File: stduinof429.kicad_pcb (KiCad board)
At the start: 2 copper layers, 94 x 56 mm, 67 parts, among them J1 Conn_02x03_Odd_Even, P1 Power, P10 CONN_02X20, P11 CONN_01X03, P12 USB_OTG, P2 Analog, P3 Digital, P4 Digital, P5 CONN_1, P6 CONN_1, P7 CONN_1, P8 CONN_1, P9 CONN_1, SW1 SW_PUSH, U1 AZ1117-3.3, U2 STM32F429IGTx

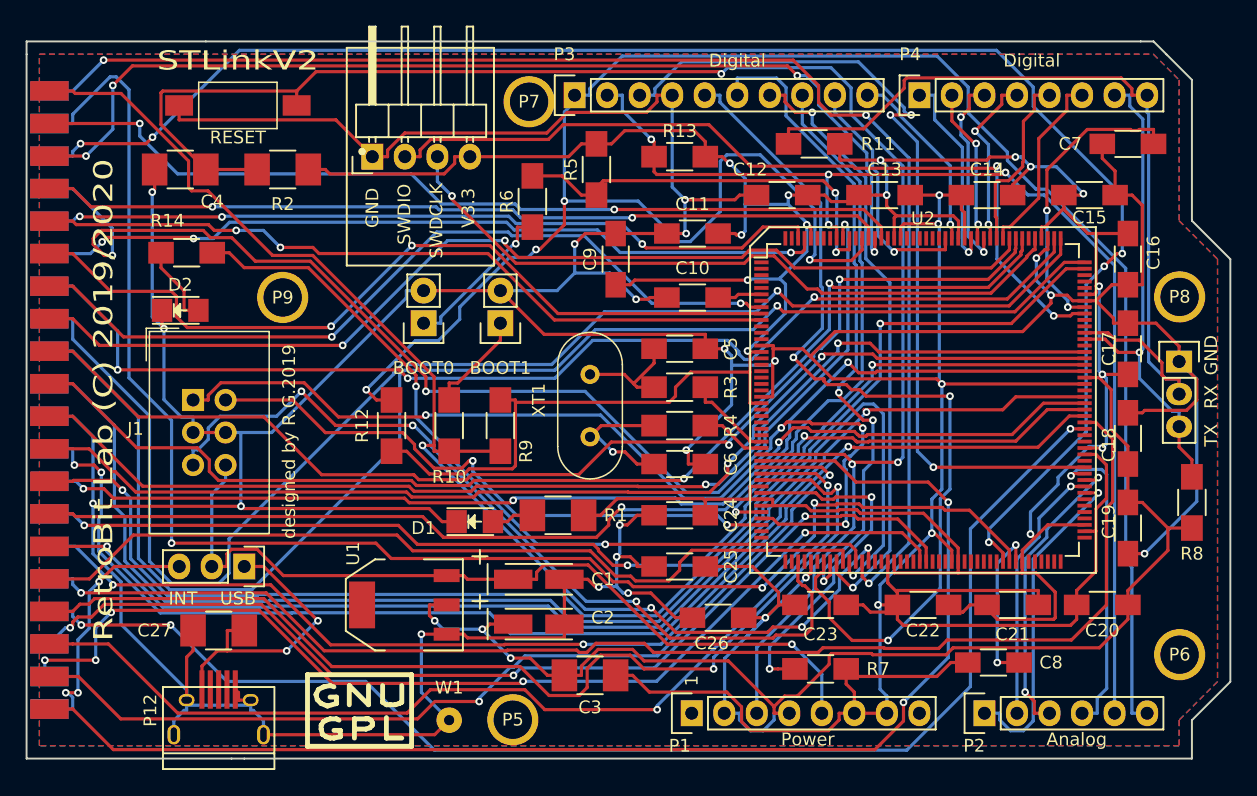
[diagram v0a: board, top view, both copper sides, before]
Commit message: Corrected pinout of lateral IDC 40 pin. Moved other bits to another port
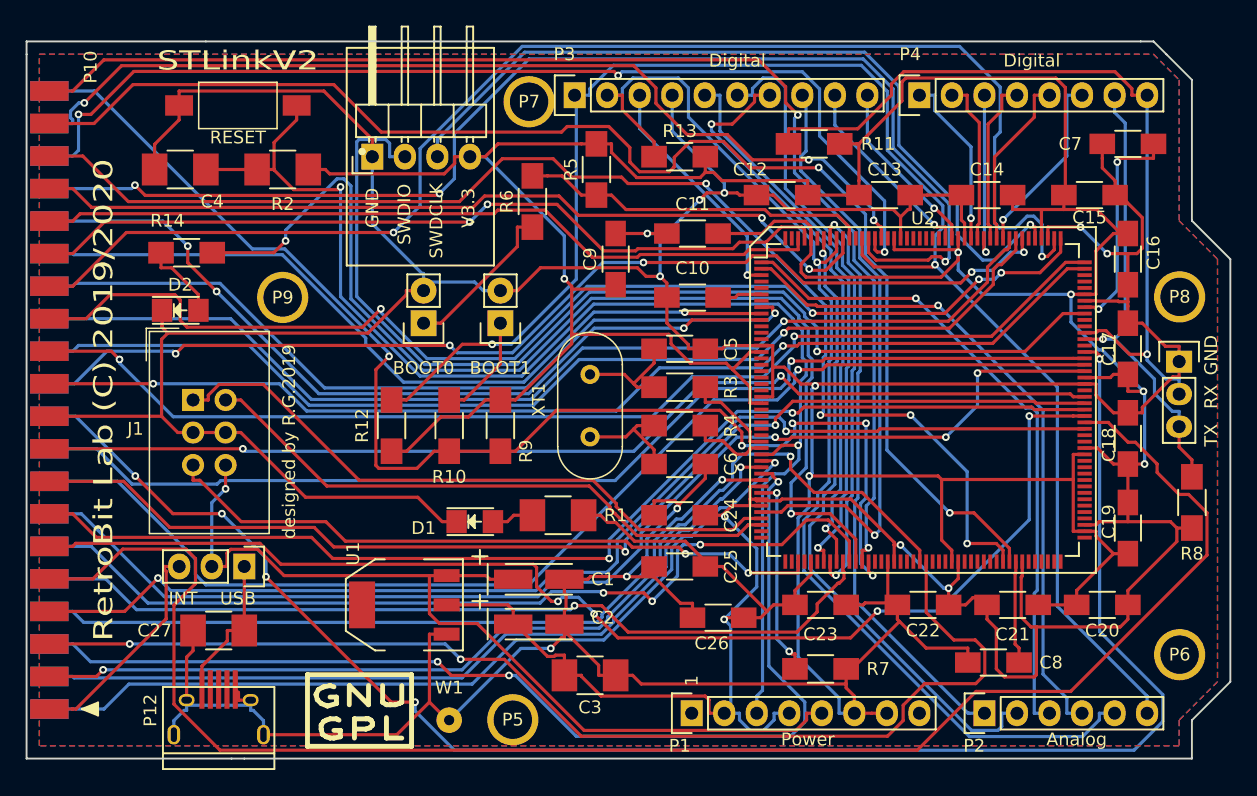
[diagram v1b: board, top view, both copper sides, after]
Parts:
- P10: moved to F.Cu
- turned P10 to 270 degrees
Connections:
- U2 pad 1: (no net) -> D10
- U2 pad 100: D12 -> (no net)
- U2 pad 169: (no net) -> D8
- U2 pad 170: (no net) -> D9
- U2 pad 2: (no net) -> D11
- U2 pad 3: (no net) -> D12
- U2 pad 96: D8 -> (no net)
- U2 pad 97: D9 -> (no net)
- U2 pad 98: D10 -> (no net)
- U2 pad 99: D11 -> (no net)
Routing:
- net GND: track 582.3 -> 475.3 mm, vias 24 -> 11
- net D12: track 66.8 -> 18.6 mm, vias 3 -> 1
- net mA9: track 89.4 -> 131.9 mm, vias 2 -> 5
- net I2C_SCL: track 160.7 -> 124.1 mm, vias 4 -> 2
- net mA0: track 103.4 -> 66.9 mm, vias 2 -> 1
- net ~mEXSEL: track 66.2 -> 96.8 mm, vias 2 -> 3
- net nRST: track 132.9 -> 102.8 mm, vias 3 -> 2
- net D9: track 20.5 -> 49.7 mm
- net SPI1_SCK: track 71.1 -> 43.1 mm, vias 3 -> 1
- net ~mMPD: track 95.2 -> 67.2 mm, vias 3 -> 2
- net D11: track 24.4 -> 52.3 mm
- net D10: track 23.4 -> 51.2 mm, vias 2 -> 1
- net ~mIRQ: track 126.8 -> 99.9 mm, vias 5 -> 4
- net mD3: track 103.3 -> 129.4 mm, vias 1 -> 0
- net SPI_SEL1: track 75.2 -> 50.3 mm, vias 4 -> 0
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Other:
- board text added: "https://github.com/gianlucarenzi/stduinof429"
- board text removed: "https://github.com/gianlucarenzi/quasiSTduino429"

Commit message: Rerouting with length match
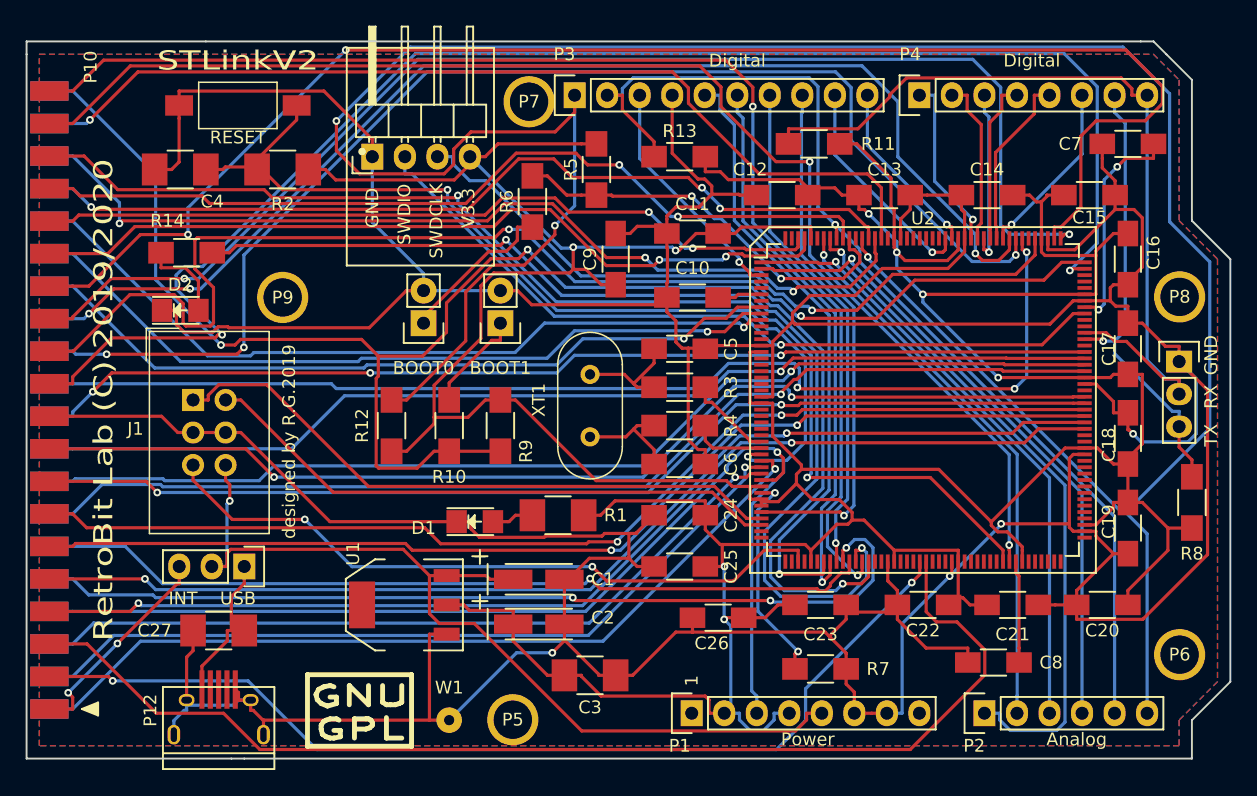
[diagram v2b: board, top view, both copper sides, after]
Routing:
- net I2C_SCL: track 124.1 -> 209.7 mm, vias 2 -> 3
- net mA9: track 131.9 -> 83.1 mm, vias 5 -> 3
- net mD3: track 129.4 -> 86.8 mm, vias 0 -> 2
- net mPHI2: track 86.3 -> 118.2 mm
- net mRD5: track 101.4 -> 130.3 mm, vias 5 -> 3
- net ~mEXSEL: track 96.8 -> 69.5 mm
- net mA2: track 84.5 -> 61.1 mm, vias 3 -> 1
- net SWDIO: track 82.8 -> 61.0 mm
- net GND: track 475.3 -> 491.5 mm, vias 11 -> 4
- net mA11: track 84.2 -> 99.0 mm, vias 1 -> 3
- net mD4: track 97.1 -> 85.7 mm, vias 4 -> 2
- net ~mS4: track 90.4 -> 100.9 mm, vias 4 -> 2
- net mA12: track 83.9 -> 94.1 mm, vias 1 -> 3
- net ~mS5: track 88.6 -> 98.3 mm
- net ~mD1XX: track 105.8 -> 114.9 mm
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
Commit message: Porting from Kicad 4 to Kicad 5
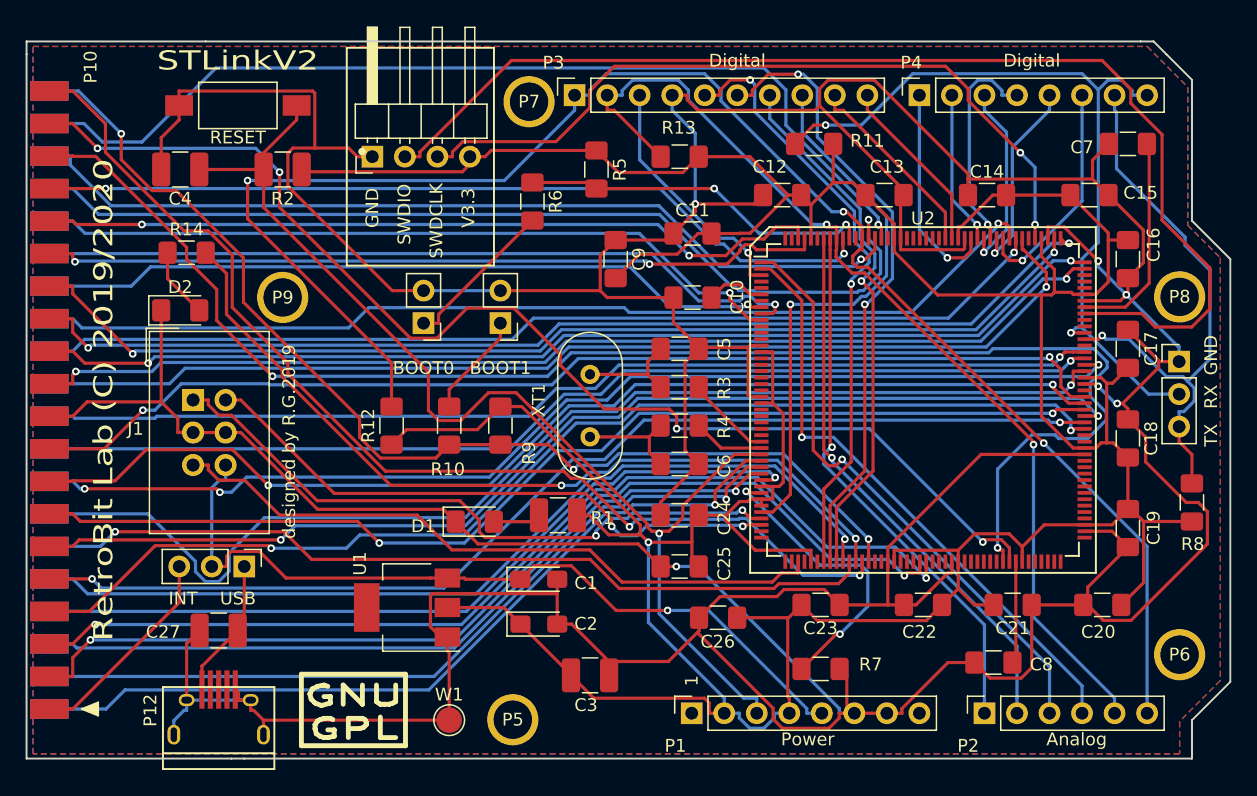
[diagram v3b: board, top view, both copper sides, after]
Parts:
- removed GPL: Symbol_GNU-GPL_CopperTop_Small, RetroBitLab:Symbol_GNU-GPL_SilkScreen_Small
- removed OSHW: OSHW-Logo2_14.6x12mm_SilkScreen, Symbol:OSHW-Logo2_14.6x12mm_SilkScreen
- added LDO: Symbol_GNU-GPL_CopperTop_Small, RetroBitLab:Symbol_GNU-GPL_SilkScreen_Small, F.Cu at (112.5, 123.8)
- added REF**: OSHW-Logo_11.4x12mm_SilkScreen, Symbol:OSHW-Logo_11.4x12mm_SilkScreen, B.Cu at (156.2, 97.4)
- BOOT0_MEM1, BOOT1_MEM1: footprint Pin_Headers:Pin_Header_Straight_1x02 -> Connector_PinHeader_2.54mm:PinHeader_1x02_P2.54mm_Vertical
- C1, C2: footprint Capacitors_Tantalum_SMD:TantalC_SizeA_EIA-3216_HandSoldering -> Capacitor_Tantalum_SMD:CP_EIA-3216-18_Kemet-A_Pad1.58x1.35mm_HandSolder
- C10, C11, C12, C13, C14, C15, C16, C17, C18, C19, C20, C21, C22, C23, C24, C25, C26, C5, C6, C7, C8, C9: footprint Capacitors_SMD:C_1206_HandSoldering -> Capacitor_SMD:C_1206_3216Metric_Pad1.42x1.75mm_HandSolder
- C27, C3, C4: footprint Capacitors_SMD:C_1210_HandSoldering -> Capacitor_SMD:C_1210_3225Metric_Pad1.42x2.65mm_HandSolder
- D1, D2: footprint LEDs:LED_1206 -> LED_SMD:LED_1206_3216Metric_Pad1.42x1.75mm_HandSolder
- DEBUG1, P11: footprint Pin_Headers:Pin_Header_Straight_1x03 -> Connector_PinHeader_2.54mm:PinHeader_1x03_P2.54mm_Vertical
- P1, P4: footprint Socket_Strips:Socket_Strip_Straight_1x08 -> Connector_PinSocket_2.54mm:PinSocket_1x08_P2.54mm_Vertical
- P2: footprint Socket_Strips:Socket_Strip_Straight_1x06 -> Connector_PinSocket_2.54mm:PinSocket_1x06_P2.54mm_Vertical
- P3: footprint Socket_Strips:Socket_Strip_Straight_1x10 -> Connector_PinSocket_2.54mm:PinSocket_1x10_P2.54mm_Vertical
- R1, R2: footprint Resistors_SMD:R_1210_HandSoldering -> Resistor_SMD:R_1210_3225Metric_Pad1.42x2.65mm_HandSolder
- R10, R11, R12, R13, R14, R3, R4, R5, R6, R7, R8, R9: footprint Resistors_SMD:R_1206_HandSoldering -> Resistor_SMD:R_1206_3216Metric_Pad1.42x1.75mm_HandSolder
- SWDIO/CLK1: footprint Pin_Headers:Pin_Header_Angled_1x04 -> Connector_PinHeader_2.54mm:PinHeader_1x04_P2.54mm_Horizontal
- U1: footprint TO_SOT_Packages_SMD:SOT-223 -> Package_TO_SOT_SMD:SOT-223
- U2: footprint Housings_QFP:LQFP-176_24x24mm_Pitch0.5mm -> Package_QFP:LQFP-176_24x24mm_P0.5mm
- W1: footprint Wire_Pads:SolderWirePad_single_0-8mmDrill -> TestPoint:TestPoint_Pad_D2.0mm
- moved U1 0.30 mm to (116.7, 115.6), turned to 180 degrees
- turned P1 to 90 degrees
- turned P2 to 90 degrees
- turned P3 to 90 degrees
- turned P4 to 90 degrees
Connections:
- P1 pad 1: (no net) -> Net-(P1-Pad1)
- P1 pad 8: (no net) -> /Vin
- P12 pad 2: (no net) -> Net-(P12-Pad2)
- P12 pad 3: (no net) -> Net-(P12-Pad3)
- P12 pad 4: (no net) -> Net-(P12-Pad4)
- P5 pad 1: (no net) -> Net-(P5-Pad1)
- P6 pad 1: (no net) -> Net-(P6-Pad1)
- P7 pad 1: (no net) -> Net-(P7-Pad1)
- P8 pad 1: (no net) -> Net-(P8-Pad1)
- P9 pad 1: (no net) -> Net-(P9-Pad1)
- U2 pad 100: (no net) -> Net-(U2-Pad100)
- U2 pad 101: (no net) -> Net-(U2-Pad101)
- U2 pad 104: (no net) -> Net-(U2-Pad104)
- U2 pad 105: (no net) -> Net-(U2-Pad105)
- U2 pad 11: (no net) -> Net-(U2-Pad11)
- U2 pad 112: (no net) -> Net-(U2-Pad112)
- U2 pad 119: (no net) -> Net-(U2-Pad119)
- U2 pad 12: (no net) -> Net-(U2-Pad12)
- U2 pad 122: (no net) -> Net-(U2-Pad122)
- U2 pad 123: (no net) -> Net-(U2-Pad123)
- U2 pad 128: (no net) -> Net-(U2-Pad128)
- U2 pad 129: (no net) -> Net-(U2-Pad129)
- U2 pad 13: (no net) -> Net-(U2-Pad13)
- U2 pad 130: (no net) -> Net-(U2-Pad130)
- U2 pad 138: (no net) -> Net-(U2-Pad138)
- U2 pad 152: (no net) -> Net-(U2-Pad152)
- U2 pad 153: (no net) -> Net-(U2-Pad153)
- U2 pad 154: (no net) -> Net-(U2-Pad154)
- U2 pad 155: (no net) -> Net-(U2-Pad155)
- U2 pad 156: (no net) -> Net-(U2-Pad156)
- U2 pad 157: (no net) -> Net-(U2-Pad157)
- U2 pad 16: (no net) -> Net-(U2-Pad16)
- U2 pad 160: (no net) -> Net-(U2-Pad160)
- U2 pad 165: (no net) -> Net-(U2-Pad165)
- U2 pad 17: (no net) -> Net-(U2-Pad17)
- U2 pad 171: (no net) -> Net-(U2-Pad171)
- U2 pad 175: (no net) -> Net-(U2-Pad175)
- U2 pad 176: (no net) -> Net-(U2-Pad176)
- U2 pad 18: (no net) -> Net-(U2-Pad18)
- U2 pad 19: (no net) -> Net-(U2-Pad19)
- U2 pad 20: (no net) -> Net-(U2-Pad20)
- U2 pad 21: (no net) -> Net-(U2-Pad21)
- U2 pad 24: (no net) -> Net-(U2-Pad24)
- U2 pad 25: (no net) -> Net-(U2-Pad25)
- U2 pad 26: (no net) -> Net-(U2-Pad26)
- U2 pad 27: (no net) -> Net-(U2-Pad27)
- U2 pad 28: (no net) -> Net-(U2-Pad28)
- U2 pad 4: (no net) -> Net-(U2-Pad4)
- U2 pad 43: (no net) -> Net-(U2-Pad43)
- U2 pad 44: (no net) -> Net-(U2-Pad44)
- U2 pad 45: (no net) -> Net-(U2-Pad45)
- U2 pad 46: (no net) -> Net-(U2-Pad46)
- U2 pad 48: (no net) -> Net-(U2-Pad48)
- U2 pad 5: (no net) -> Net-(U2-Pad5)
- U2 pad 50: (no net) -> Net-(U2-Pad50)
- U2 pad 59: (no net) -> Net-(U2-Pad59)
- U2 pad 60: (no net) -> Net-(U2-Pad60)
- U2 pad 63: (no net) -> Net-(U2-Pad63)
- U2 pad 64: (no net) -> Net-(U2-Pad64)
- U2 pad 65: (no net) -> Net-(U2-Pad65)
- U2 pad 68: (no net) -> Net-(U2-Pad68)
- U2 pad 69: (no net) -> Net-(U2-Pad69)
- U2 pad 7: (no net) -> Net-(U2-Pad7)
- U2 pad 70: (no net) -> Net-(U2-Pad70)
- U2 pad 73: (no net) -> Net-(U2-Pad73)
- U2 pad 74: (no net) -> Net-(U2-Pad74)
- U2 pad 75: (no net) -> Net-(U2-Pad75)
- U2 pad 76: (no net) -> Net-(U2-Pad76)
- U2 pad 77: (no net) -> Net-(U2-Pad77)
- U2 pad 78: (no net) -> Net-(U2-Pad78)
- U2 pad 83: (no net) -> Net-(U2-Pad83)
- U2 pad 84: (no net) -> Net-(U2-Pad84)
- U2 pad 85: (no net) -> Net-(U2-Pad85)
- U2 pad 86: (no net) -> Net-(U2-Pad86)
- U2 pad 87: (no net) -> Net-(U2-Pad87)
- U2 pad 88: (no net) -> Net-(U2-Pad88)
- U2 pad 89: (no net) -> Net-(U2-Pad89)
- U2 pad 92: (no net) -> Net-(U2-Pad92)
- U2 pad 93: (no net) -> Net-(U2-Pad93)
- U2 pad 94: (no net) -> Net-(U2-Pad94)
- U2 pad 95: (no net) -> Net-(U2-Pad95)
- U2 pad 96: (no net) -> Net-(U2-Pad96)
- U2 pad 97: (no net) -> Net-(U2-Pad97)
- U2 pad 98: (no net) -> Net-(U2-Pad98)
- U2 pad 99: (no net) -> Net-(U2-Pad99)
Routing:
- net I2C_SCL: track 209.7 -> 128.5 mm
- net VCC_3V3: track 397.2 -> 336.9 mm, vias 8 -> 1
- net mRD5: track 130.3 -> 86.2 mm
- net mPHI2: track 118.2 -> 85.1 mm
- net SWDIO: track 61.0 -> 91.5 mm, vias 1 -> 0
- net ~mD1XX: track 114.9 -> 85.4 mm
- net ~mIRQ: track 94.7 -> 116.6 mm
- net GND: track 491.5 -> 512.2 mm, vias 4 -> 6
- net mA11: track 99.0 -> 79.7 mm, vias 3 -> 1
- net LEDGRN_MEM: track 83.7 -> 65.6 mm
- net ~mRST: track 100.6 -> 84.8 mm
- net ~mS4: track 100.9 -> 85.4 mm
- net mA12: track 94.1 -> 80.1 mm, vias 3 -> 1
- net ~mS5: track 98.3 -> 84.6 mm
- net mD1: track 90.6 -> 78.4 mm, vias 0 -> 2
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
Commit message: Added without the packages/kicad folder needed. All stuff is now on kicad sources and RetroBitLab Library
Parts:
- removed LDO: Symbol_GNU-GPL_CopperTop_Small, RetroBitLab:Symbol_GNU-GPL_SilkScreen_Small
- removed REF**: OSHW-Logo_11.4x12mm_SilkScreen, Symbol:OSHW-Logo_11.4x12mm_SilkScreen

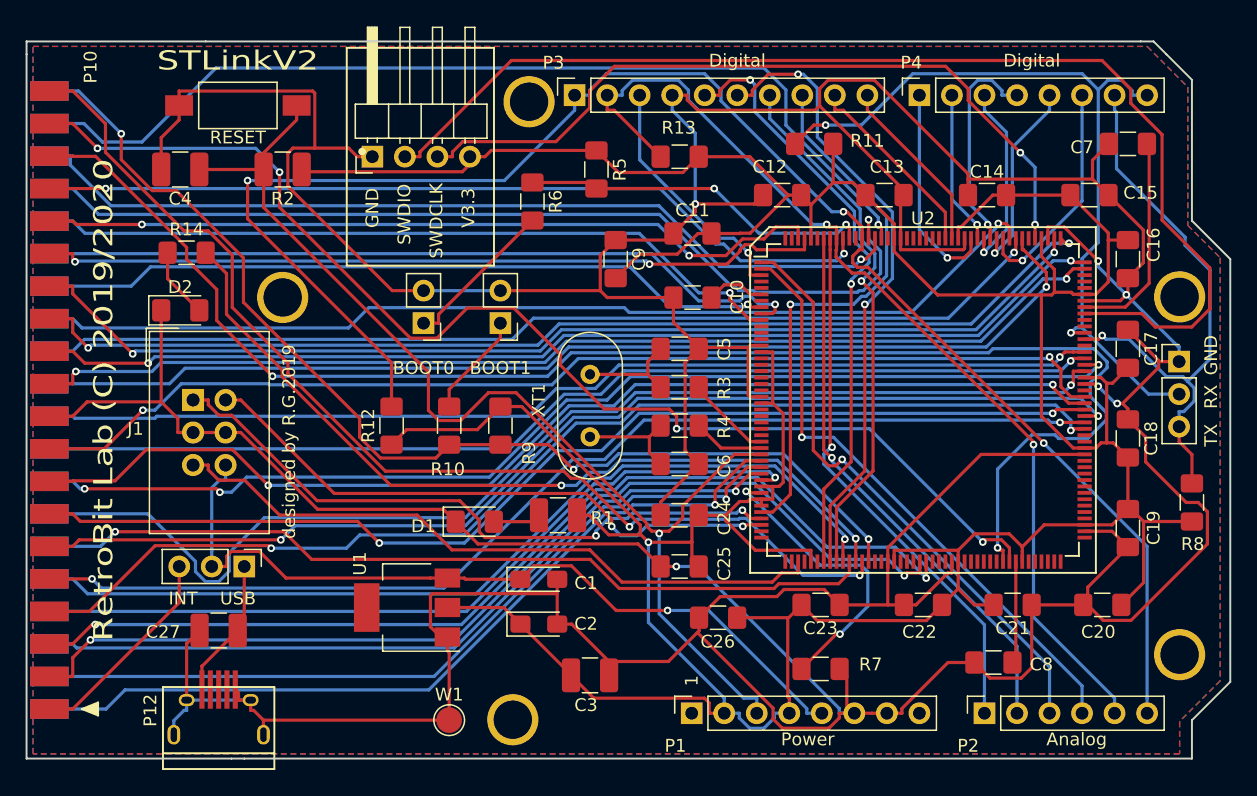
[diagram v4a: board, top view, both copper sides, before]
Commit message: Modified for Kicad 5.1.9
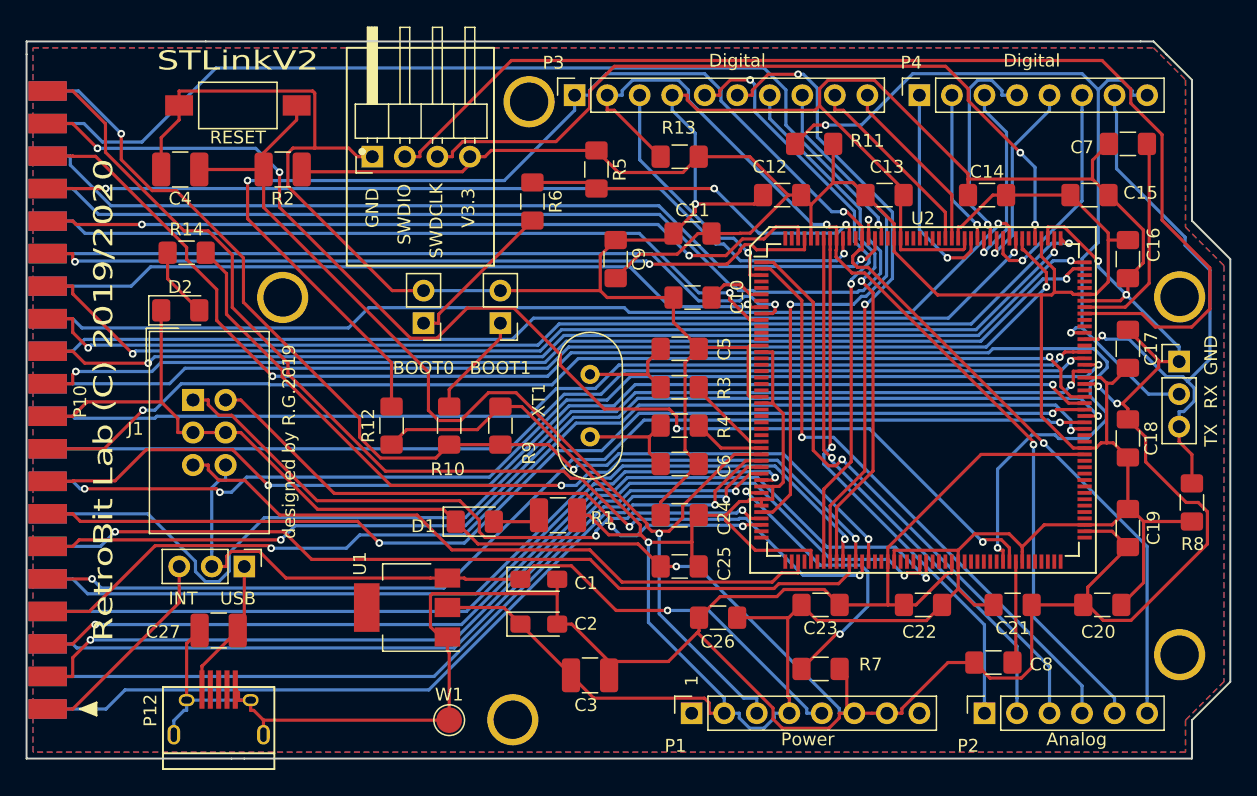
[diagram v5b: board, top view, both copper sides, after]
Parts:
- P10: value CONN_02X20 -> Conn_02x20_Odd_Even
- moved P10 0.13 mm to (86.9, 99.4)

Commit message: Created for rescue :-(
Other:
- board text added: "RetroBit Lab (C) 2019/2021"
- board text added: "designed by R.G.2021"
- board text removed: "RetroBit Lab (C) 2019/2020"
- board text removed: "designed by R.G.2019"
